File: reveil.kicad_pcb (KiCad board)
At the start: 2 copper layers, 170 x 90 mm, 26 parts, among them Q1 2N3904, Q2 IRF540N, SW1 SW_SPDT, U1 MAX7219, U2 MAX7219

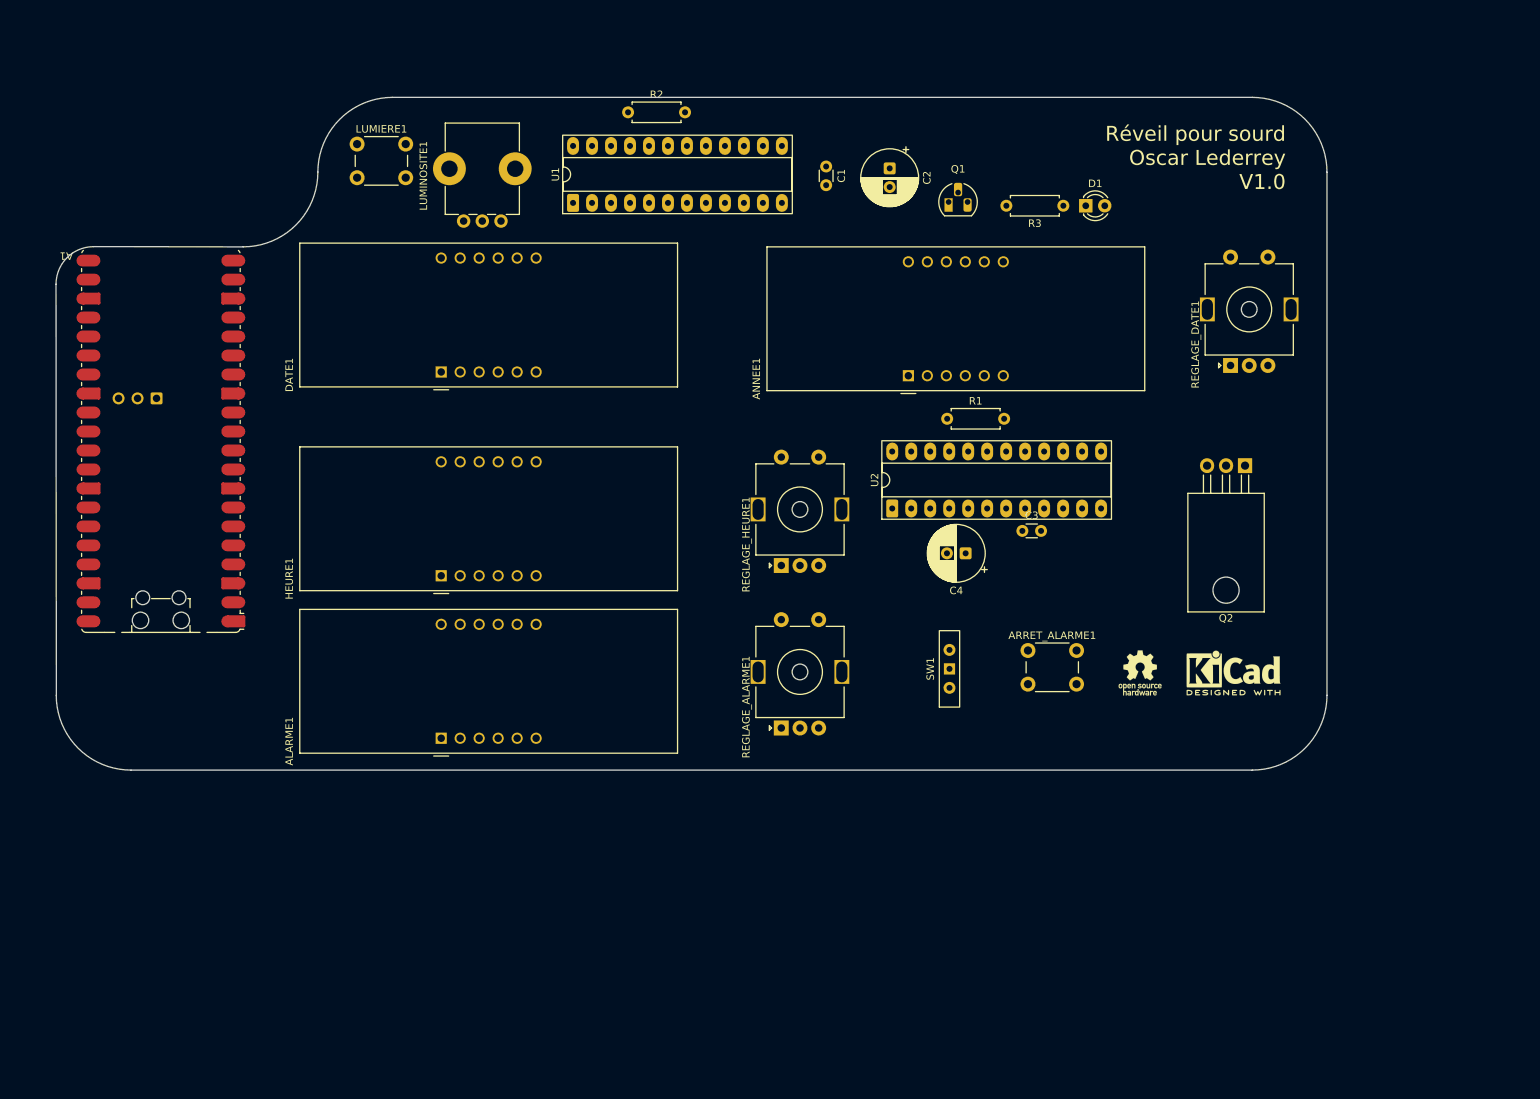
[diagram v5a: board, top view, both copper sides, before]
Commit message: all footprints and placements
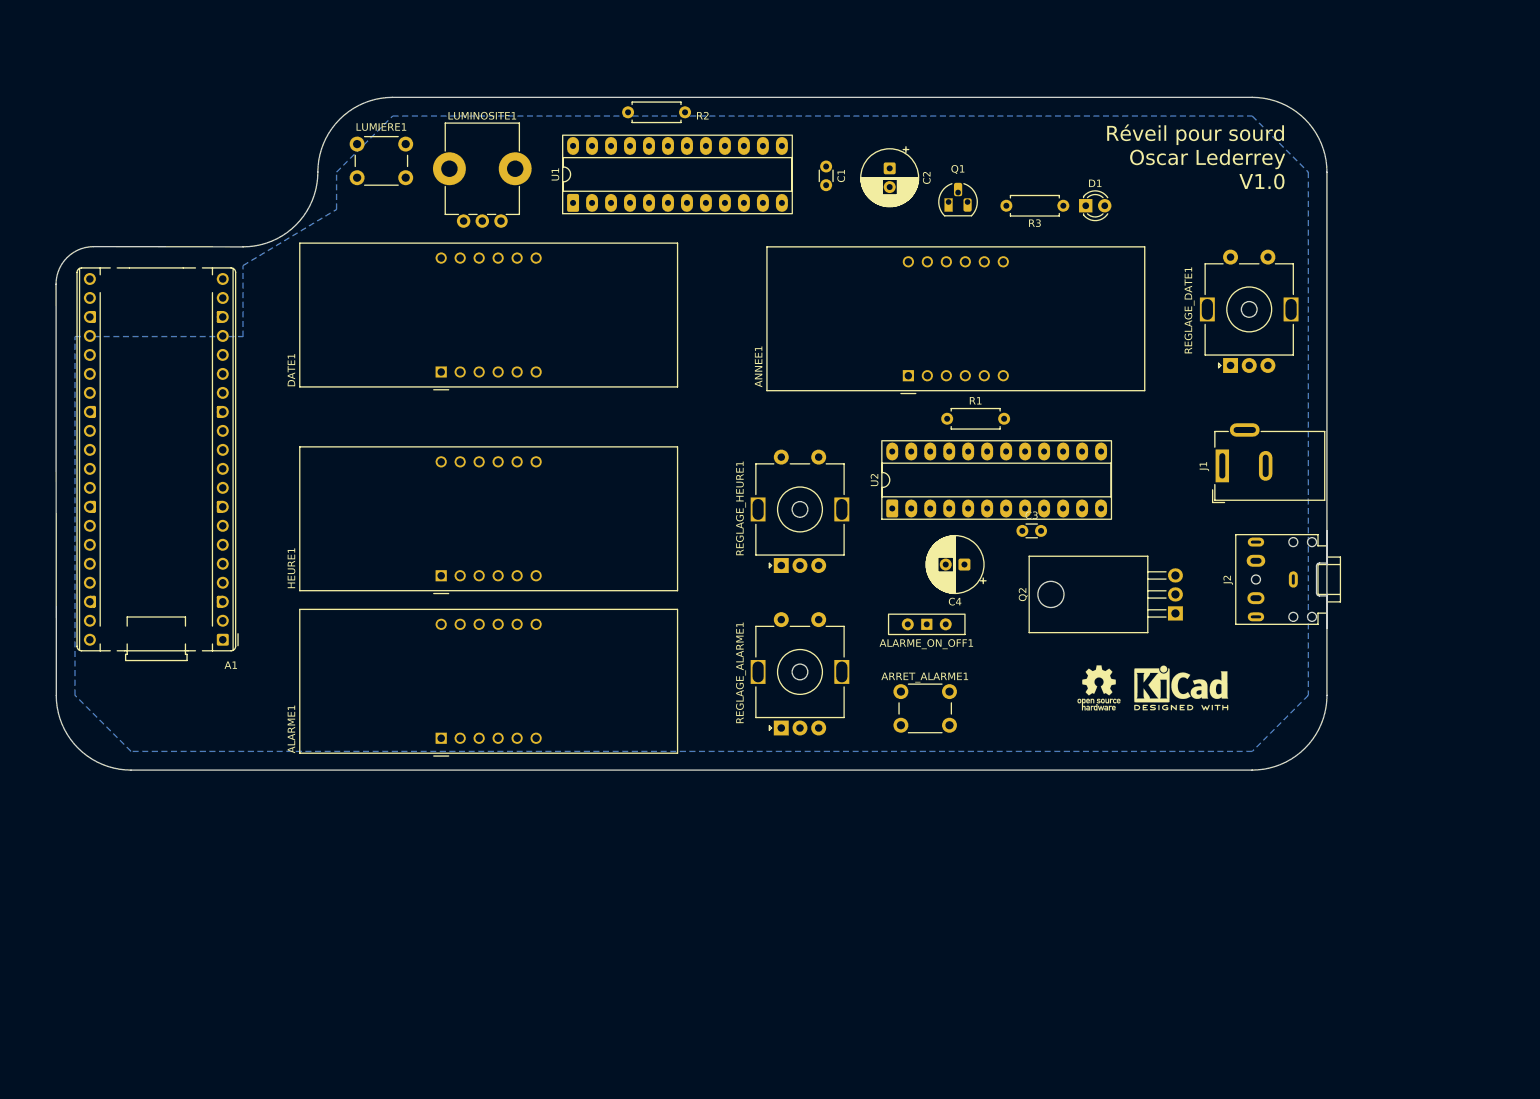
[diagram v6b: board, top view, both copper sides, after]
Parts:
- added J1: Barrel_Jack_Switch, Connector_BarrelJack:BarrelJack_Wuerth_6941xx301002, F.Cu at (236.0, 69.3)
- added J2: AudioJack3_SwitchTR, Connector_Audio:Jack_3.5mm_CUI_SJ1-3525N_Horizontal, F.Cu at (245.5, 84.5)
- A1: footprint Module:RaspberryPi_Pico_W_SMD_HandSolder -> Module:RaspberryPi_Pico_Common_THT
- moved A1 27.8 mm to (102.3, 92.6)
- moved Q2 21.9 mm to (229.7, 89.0), turned to 90 degrees
- moved ARRET_ALARME1 17.9 mm to (193.0, 99.5)
- moved REF** 7.28 mm to (230.5, 99.0)
- moved ALARME_ON_OFF1 6.69 mm to (196.5, 90.5), turned to 180 degrees
- moved REF** 5.85 mm to (219.5, 99.0)
- moved C4 1.51 mm to (201.5, 82.5)
- renumbered SW1 to ALARME_ON_OFF1
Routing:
- added copper zone on B.Cu, net GND

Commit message: routing completed
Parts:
- moved C3 1.00 mm to (209.2, 79.0)
- renumbered REF** to LOGO1, REF** to LOGO2
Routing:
- net VBUS: track 0.00 -> 322.7 mm
- net VIBREUR: track 0.00 -> 190.1 mm, vias 0 -> 1
- net +3V3: track 0.00 -> 171.7 mm, vias 0 -> 2
- net ARRET_ALARME: track 0.00 -> 166.8 mm, vias 0 -> 1
- net REGLAGE_DATE_S: track 0.00 -> 159.5 mm, vias 0 -> 1
- net REGLAGE_DATE_A: track 0.00 -> 155.5 mm, vias 0 -> 1
- net REGLAGE_DATE_B: track 0.00 -> 154.3 mm, vias 0 -> 1
- net ALARME_ON_OFF: track 0.00 -> 144.3 mm, vias 0 -> 1
- net REGLAGE_ALARME_B: track 0.00 -> 138.4 mm, vias 0 -> 1
- net REGLAGE_ALARME_A: track 0.00 -> 126.5 mm, vias 0 -> 1
- net REGLAGE_ALARME_S: track 0.00 -> 125.0 mm, vias 0 -> 1
- net LED: track 0.00 -> 123.8 mm
- net HEURE_ALARME_LOAD: track 0.00 -> 120.8 mm
- net HEURE_ALARME_CLK: track 0.00 -> 120.7 mm
- net Net-(ALARME1-a): track 0.00 -> 109.4 mm
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- added copper zone on F.Cu, net VBUS

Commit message: fixed outline
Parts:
- added H1: MountingHole, MountingHole:MountingHole_4.3mm_M4, F.Cu at (230.0, 35.0)
- added H2: MountingHole, MountingHole:MountingHole_4.3mm_M4, F.Cu at (210.5, 102.0)
- added H3: MountingHole, MountingHole:MountingHole_4.3mm_M4, F.Cu at (107.5, 99.0)
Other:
- outline, holes or cut-outs redrawn
